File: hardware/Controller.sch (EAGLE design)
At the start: 70 parts, among them Q1 MOSFET-NCHANNEL2N7002PW, Q2 BSS84PW, Q3 BSS84PW, U3 MMA8652FC, U4 MCP6002MS, U5 TXS0101DCK, U6 LCD_1.8, U7 VREG

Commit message: hardware: Change in resistor values in analog section
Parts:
- C12: value 15p -> 470p
- R16, R17: value 1M -> 100k
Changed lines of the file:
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@@
 <part name="GUITAR" library="SparkFun-Connectors" deviceset="M02" device="LOCK" value="M02LOCK"/>
 <part name="R13" library="SparkFun-Resistors" deviceset="RESISTOR" device="0603" value="1M"/>
-<part name="R17" library="SparkFun-Resistors" deviceset="RESISTOR" device="0603" value="1M"/>
-<part name="R16" library="SparkFun-Resistors" deviceset="RESISTOR" device="0603" value="1M"/>
+<part name="R17" library="SparkFun-Resistors" deviceset="RESISTOR" device="0603" value="100k"/>
+<part name="R16" library="SparkFun-Resistors" deviceset="RESISTOR" device="0603" value="100k"/>
 <part name="KNOB" library="SparkFun-Connectors" deviceset="M04" device="LOCK"/>
 <part name="GND17" library="SparkFun" deviceset="GND" device=""/>
@@
 <part name="P+7" library="SparkFun" deviceset="3.3V" device=""/>
 <part name="SH1" library="Parts" deviceset="SHORT" device=""/>
-<part name="C12" library="SparkFun-Capacitors" deviceset="CAP" device="0603-CAP" value="15p"/>
+<part name="C12" library="SparkFun-Capacitors" deviceset="CAP" device="0603-CAP" value="470p"/>
 </parts>
 <sheets>

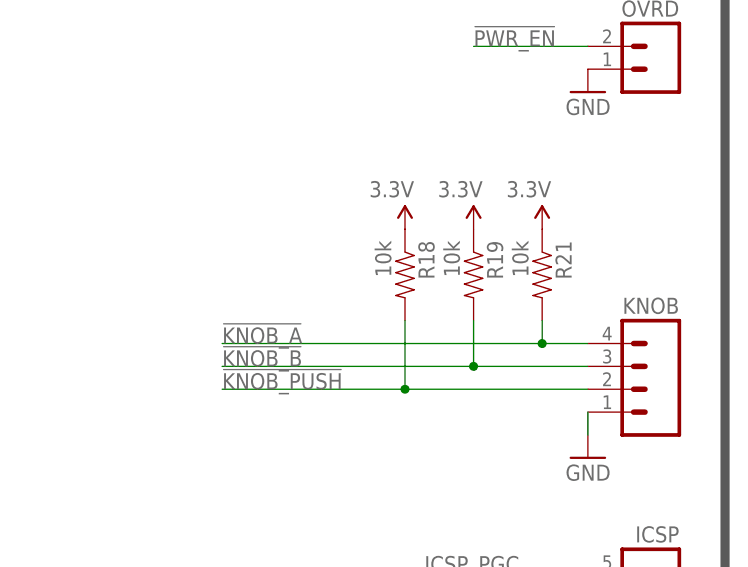
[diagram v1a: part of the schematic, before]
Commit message: hardware: Remove R18
It was wrong to pull to 3.3V behind the diode, resulting in always enabling the VREG
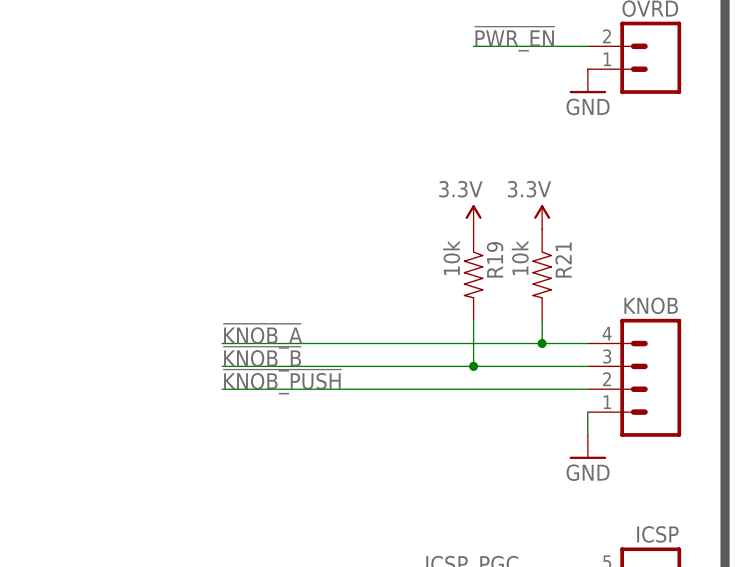
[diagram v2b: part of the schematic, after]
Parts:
- removed R18: 10k, SparkFun-Resistors:RESISTOR0603
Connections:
- net !KNOB_PUSH: no longer R18.2
- net 3.3V: no longer R18.1
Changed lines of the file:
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@@
 <part name="C11" library="SparkFun-Capacitors" deviceset="CAP" device="0603-CAP" value="1u"/>
 <part name="C9" library="SparkFun-Capacitors" deviceset="CAP" device="0603-CAP" value="1u"/>
-<part name="R18" library="SparkFun-Resistors" deviceset="RESISTOR" device="0603" value="10k"/>
 <part name="R19" library="SparkFun-Resistors" deviceset="RESISTOR" device="0603" value="10k"/>
 <part name="R21" library="SparkFun-Resistors" deviceset="RESISTOR" device="0603" value="10k"/>
-<part name="P+12" library="SparkFun" deviceset="3.3V" device=""/>
 <part name="P+13" library="SparkFun" deviceset="3.3V" device=""/>
 <part name="P+14" library="SparkFun" deviceset="3.3V" device=""/>
@@
 <instance part="C11" gate="G$1" x="274.32" y="139.7"/>
 <instance part="C9" gate="G$1" x="246.38" y="111.76" rot="R90"/>
-<instance part="R18" gate="G$1" x="419.1" y="226.06" rot="R270"/>
 <instance part="R19" gate="G$1" x="426.72" y="226.06" rot="R270"/>
 <instance part="R21" gate="G$1" x="434.34" y="226.06" rot="R270"/>
-<instance part="P+12" gate="G$1" x="419.1" y="231.14" rot="MR0"/>
 <instance part="P+13" gate="G$1" x="426.72" y="231.14" rot="MR0"/>
 <instance part="P+14" gate="G$1" x="434.34" y="231.14" rot="MR0"/>
@@
 </segment>
 <segment>
-<pinref part="R18" gate="G$1" pin="1"/>
-<pinref part="P+12" gate="G$1" pin="3.3V"/>
-</segment>
-<segment>
 <pinref part="R19" gate="G$1" pin="1"/>
 <pinref part="P+13" gate="G$1" pin="3.3V"/>
@@
 <net name="!KNOB_PUSH" class="0">
 <segment>
-<wire x1="398.78" y1="213.36" x2="419.1" y2="213.36" width="0.1524" layer="91"/>
 <label x="398.78" y="213.36" size="1.778" layer="95"/>
 <pinref part="KNOB" gate="G$1" pin="2"/>
-<wire x1="419.1" y1="220.98" x2="419.1" y2="213.36" width="0.1524" layer="91"/>
-<wire x1="419.1" y1="213.36" x2="439.42" y2="213.36" width="0.1524" layer="91"/>
-<pinref part="R18" gate="G$1" pin="2"/>
-<junction x="419.1" y="213.36"/>
-</segment>
-<segment>
+<wire x1="398.78" y1="213.36" x2="439.42" y2="213.36" width="0.1524" layer="91"/>
+</segment>
+<segment>

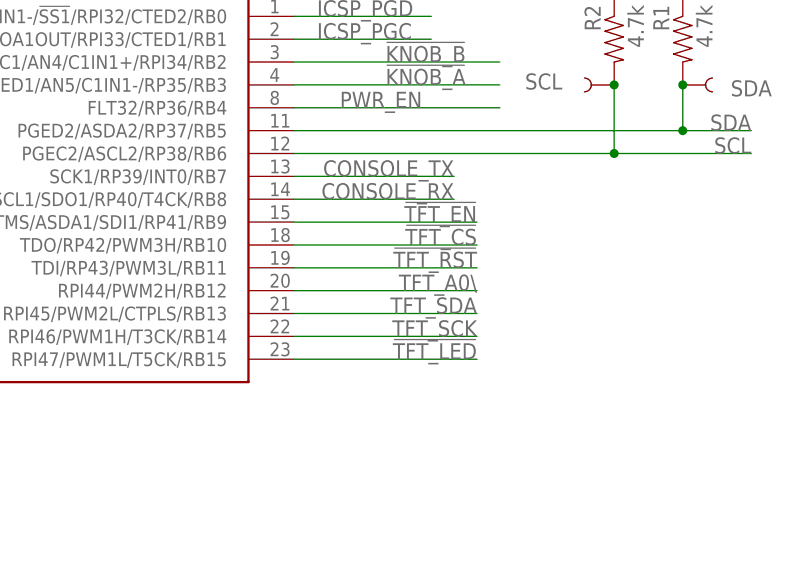
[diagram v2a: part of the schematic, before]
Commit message: hardware: Route TFT SPI pins to RPx pins
Previously, the MCU pins used for TFT SPI could not be driven by a SPI peripheral.
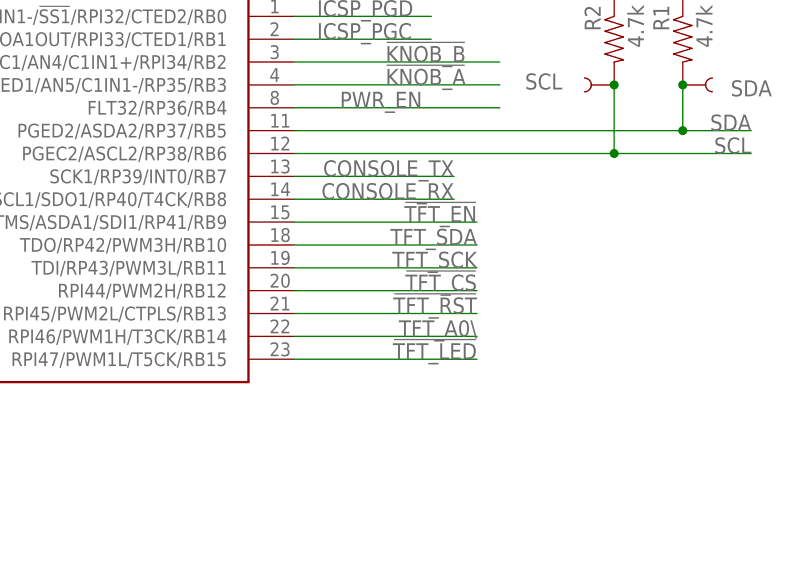
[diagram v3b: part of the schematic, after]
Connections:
- net !TFT_CS: now also U1.RPI44/PWM2H/RB12; no longer U1.TDO/RP42/PWM3H/RB10
- net !TFT_RST: now also U1.RPI45/PWM2L/CTPLS/RB13; no longer U1.TDI/RP43/PWM3L/RB11
- net TFT_A0\: now also U1.RPI46/PWM1H/T3CK/RB14; no longer U1.RPI44/PWM2H/RB12
- net TFT_SCK: now also U1.TDI/RP43/PWM3L/RB11; no longer U1.RPI46/PWM1H/T3CK/RB14
- net TFT_SDA: now also U1.TDO/RP42/PWM3H/RB10; no longer U1.RPI45/PWM2L/CTPLS/RB13
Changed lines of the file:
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@@
 </segment>
 <segment>
-<wire x1="152.4" y1="45.72" x2="172.72" y2="45.72" width="0.1524" layer="91"/>
-<label x="172.72" y="45.72" size="1.778" layer="95" rot="MR0"/>
-<pinref part="U1" gate="G$1" pin="TDI/RP43/PWM3L/RB11"/>
+<label x="172.72" y="40.64" size="1.778" layer="95" rot="MR0"/>
+<wire x1="152.4" y1="40.64" x2="172.72" y2="40.64" width="0.1524" layer="91"/>
+<pinref part="U1" gate="G$1" pin="RPI45/PWM2L/CTPLS/RB13"/>
 </segment>
 </net>
@@
 </segment>
 <segment>
-<wire x1="152.4" y1="43.18" x2="172.72" y2="43.18" width="0.1524" layer="91"/>
-<label x="172.72" y="43.18" size="1.778" layer="95" rot="MR0"/>
-<pinref part="U1" gate="G$1" pin="RPI44/PWM2H/RB12"/>
+<label x="172.72" y="38.1" size="1.778" layer="95" rot="MR0"/>
+<wire x1="152.4" y1="38.1" x2="172.72" y2="38.1" width="0.1524" layer="91"/>
+<pinref part="U1" gate="G$1" pin="RPI46/PWM1H/T3CK/RB14"/>
 </segment>
 </net>
@@
 </segment>
 <segment>
-<wire x1="152.4" y1="40.64" x2="172.72" y2="40.64" width="0.1524" layer="91"/>
-<label x="172.72" y="40.64" size="1.778" layer="95" rot="MR0"/>
-<pinref part="U1" gate="G$1" pin="RPI45/PWM2L/CTPLS/RB13"/>
+<label x="172.72" y="48.26" size="1.778" layer="95" rot="MR0"/>
+<wire x1="152.4" y1="48.26" x2="172.72" y2="48.26" width="0.1524" layer="91"/>
+<pinref part="U1" gate="G$1" pin="TDO/RP42/PWM3H/RB10"/>
 </segment>
 </net>
@@
 </segment>
 <segment>
-<wire x1="152.4" y1="38.1" x2="172.72" y2="38.1" width="0.1524" layer="91"/>
-<label x="172.72" y="38.1" size="1.778" layer="95" rot="MR0"/>
-<pinref part="U1" gate="G$1" pin="RPI46/PWM1H/T3CK/RB14"/>
+<label x="172.72" y="45.72" size="1.778" layer="95" rot="MR0"/>
+<wire x1="152.4" y1="45.72" x2="172.72" y2="45.72" width="0.1524" layer="91"/>
+<pinref part="U1" gate="G$1" pin="TDI/RP43/PWM3L/RB11"/>
 </segment>
 </net>
@@
 </segment>
 <segment>
-<wire x1="152.4" y1="48.26" x2="172.72" y2="48.26" width="0.1524" layer="91"/>
-<label x="172.72" y="48.26" size="1.778" layer="95" rot="MR0"/>
-<pinref part="U1" gate="G$1" pin="TDO/RP42/PWM3H/RB10"/>
+<label x="172.72" y="43.18" size="1.778" layer="95" rot="MR0"/>
+<wire x1="152.4" y1="43.18" x2="172.72" y2="43.18" width="0.1524" layer="91"/>
+<pinref part="U1" gate="G$1" pin="RPI44/PWM2H/RB12"/>
 </segment>
 </net>

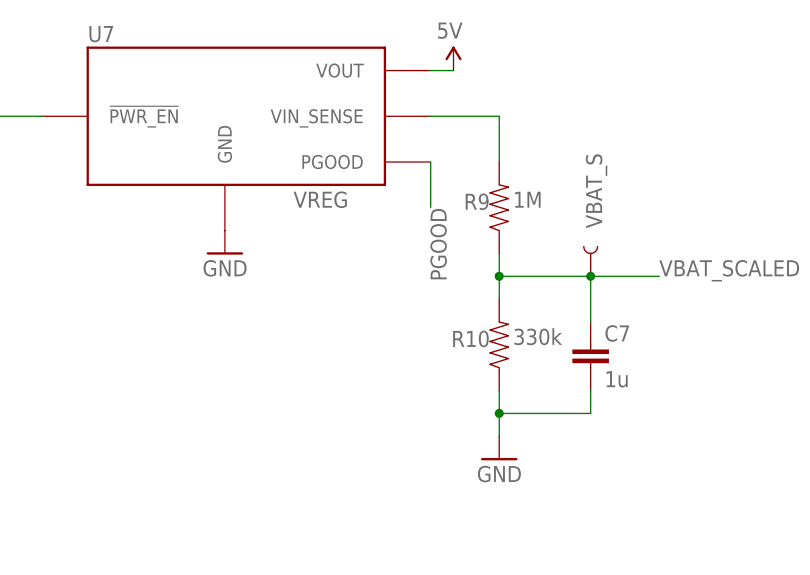
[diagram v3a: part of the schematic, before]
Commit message: hardware: divide PGOOD to be 3.3V
It is a 5V signal, previously fed into a non-5V tolerant pin.
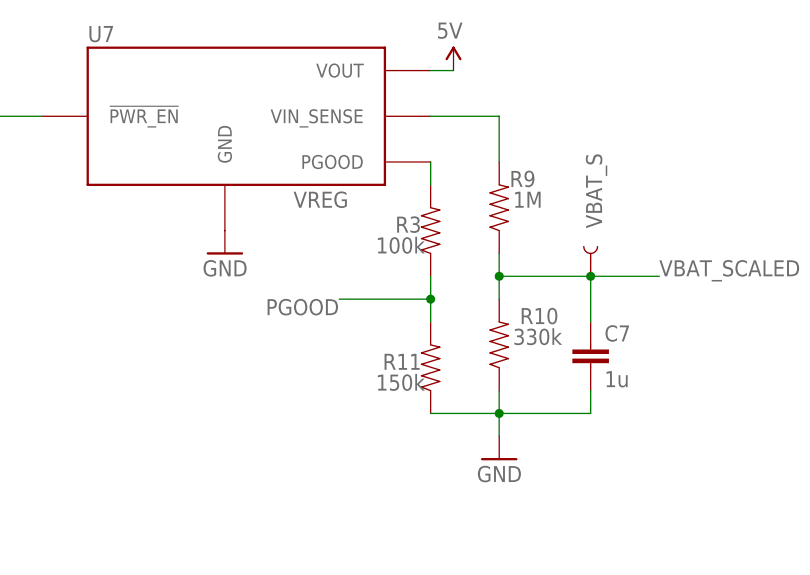
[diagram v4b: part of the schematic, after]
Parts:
- added R11: 150k, SparkFun-Resistors:RESISTOR0603
- added R3: 100k, SparkFun-Resistors:RESISTOR0603
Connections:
- new net N$8: R3.2, U7.PGOOD
- net GND: now also R11.1
- net PGOOD: now also R11.2, R3.1; no longer U7.PGOOD
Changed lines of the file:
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@@
 <part name="SH1" library="Parts" deviceset="SHORT" device=""/>
 <part name="C12" library="SparkFun-Capacitors" deviceset="CAP" device="0603-CAP" value="470p"/>
+<part name="R3" library="SparkFun-Resistors" deviceset="RESISTOR" device="0603" value="100k"/>
+<part name="R11" library="SparkFun-Resistors" deviceset="RESISTOR" device="0603" value="150k"/>
 </parts>
 <sheets>
@@
 <instance part="U1" gate="G$1" x="76.2" y="60.96"/>
 <instance part="R9" gate="G$1" x="71.12" y="233.68" smashed="yes" rot="R90">
-<attribute name="NAME" x="70.104" y="235.2294" size="1.778" layer="95" rot="R180"/>
+<attribute name="NAME" x="75.184" y="237.7694" size="1.778" layer="95" rot="R180"/>
 <attribute name="VALUE" x="72.644" y="233.68" size="1.778" layer="96"/>
 </instance>
 <instance part="R10" gate="G$1" x="71.12" y="218.44" smashed="yes" rot="R90">
-<attribute name="NAME" x="70.104" y="219.9894" size="1.778" layer="95" rot="R180"/>
+<attribute name="NAME" x="77.724" y="222.5294" size="1.778" layer="95" rot="R180"/>
 <attribute name="VALUE" x="72.644" y="218.44" size="1.778" layer="96"/>
 </instance>
@@
 <instance part="SH1" gate="G$1" x="152.4" y="162.56"/>
 <instance part="C12" gate="G$1" x="264.16" y="96.52" rot="R180"/>
+<instance part="R3" gate="G$1" x="63.5" y="231.14" smashed="yes" rot="R90">
+<attribute name="NAME" x="62.484" y="232.6894" size="1.778" layer="95" rot="R180"/>
+<attribute name="VALUE" x="57.404" y="228.6" size="1.778" layer="96"/>
+</instance>
+<instance part="R11" gate="G$1" x="63.5" y="215.9" smashed="yes" rot="R90">
+<attribute name="NAME" x="62.484" y="217.4494" size="1.778" layer="95" rot="R180"/>
+<attribute name="VALUE" x="57.404" y="213.36" size="1.778" layer="96"/>
+</instance>
 </instances>
 <busses>
@@
 <wire x1="81.28" y1="210.82" x2="71.12" y2="210.82" width="0.1524" layer="91"/>
 <junction x="71.12" y="210.82"/>
+<pinref part="R11" gate="G$1" pin="1"/>
+<wire x1="63.5" y1="210.82" x2="71.12" y2="210.82" width="0.1524" layer="91"/>
 </segment>
 <segment>
@@
 </segment>
 <segment>
-<wire x1="63.5" y1="238.76" x2="63.5" y2="233.68" width="0.1524" layer="91"/>
-<label x="63.5" y="233.68" size="1.778" layer="95" rot="R270"/>
-<pinref part="U7" gate="G$1" pin="PGOOD"/>
+<label x="53.34" y="223.52" size="1.778" layer="95" rot="R180"/>
+<wire x1="63.5" y1="223.52" x2="53.34" y2="223.52" width="0.1524" layer="91"/>
+<pinref part="R3" gate="G$1" pin="1"/>
+<pinref part="R11" gate="G$1" pin="2"/>
+<wire x1="63.5" y1="226.06" x2="63.5" y2="223.52" width="0.1524" layer="91"/>
+<junction x="63.5" y="223.52"/>
+<wire x1="63.5" y1="223.52" x2="63.5" y2="220.98" width="0.1524" layer="91"/>
 </segment>
 </net>
@@
 </segment>
 </net>
+<net name="N$8" class="0">
+<segment>
+<pinref part="U7" gate="G$1" pin="PGOOD"/>
+<pinref part="R3" gate="G$1" pin="2"/>
+<wire x1="63.5" y1="238.76" x2="63.5" y2="236.22" width="0.1524" layer="91"/>
+</segment>
+</net>
